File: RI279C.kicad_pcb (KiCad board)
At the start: 2 copper layers, 48.3 x 39.4 mm, 10 parts, among them J1 Ribbon Cable, J2 Multiway, J3 Meter

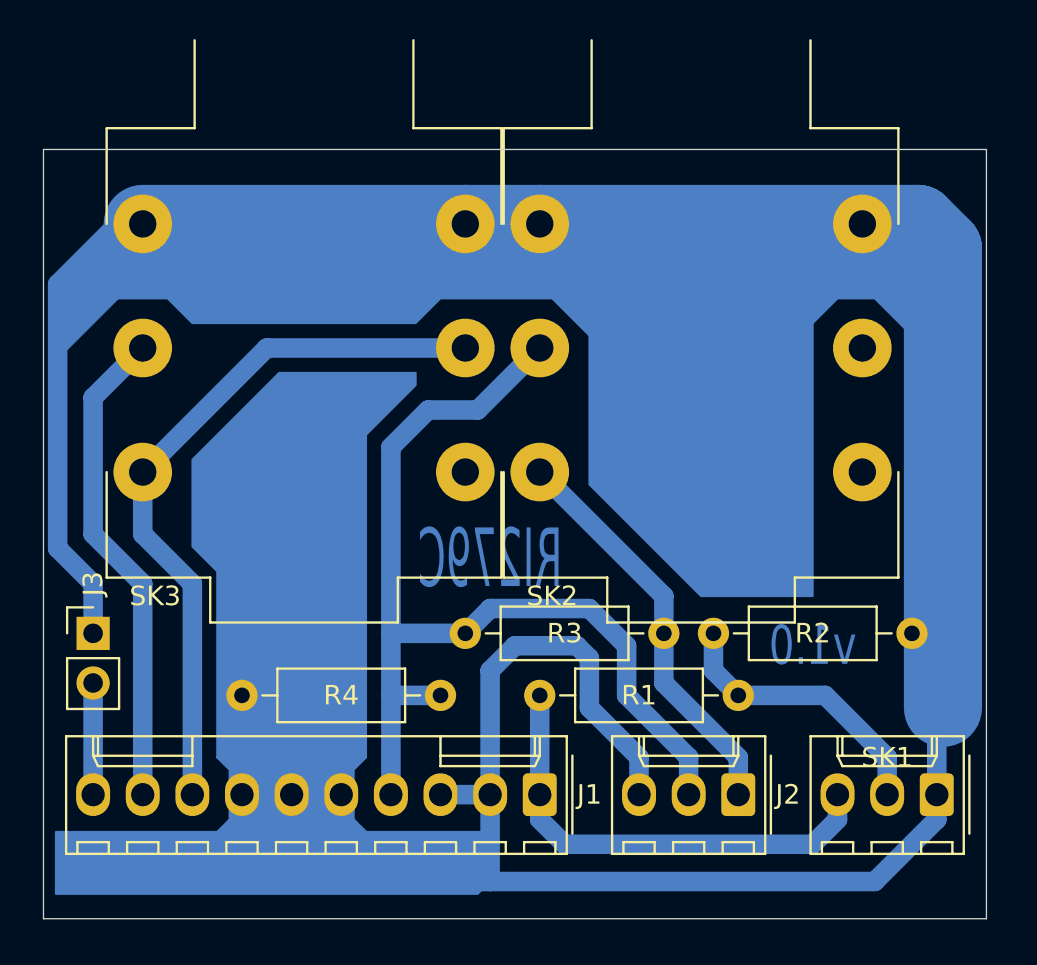
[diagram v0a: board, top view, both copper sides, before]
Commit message: aligned edge cuts to mm grid, 39 mm x 49 mm
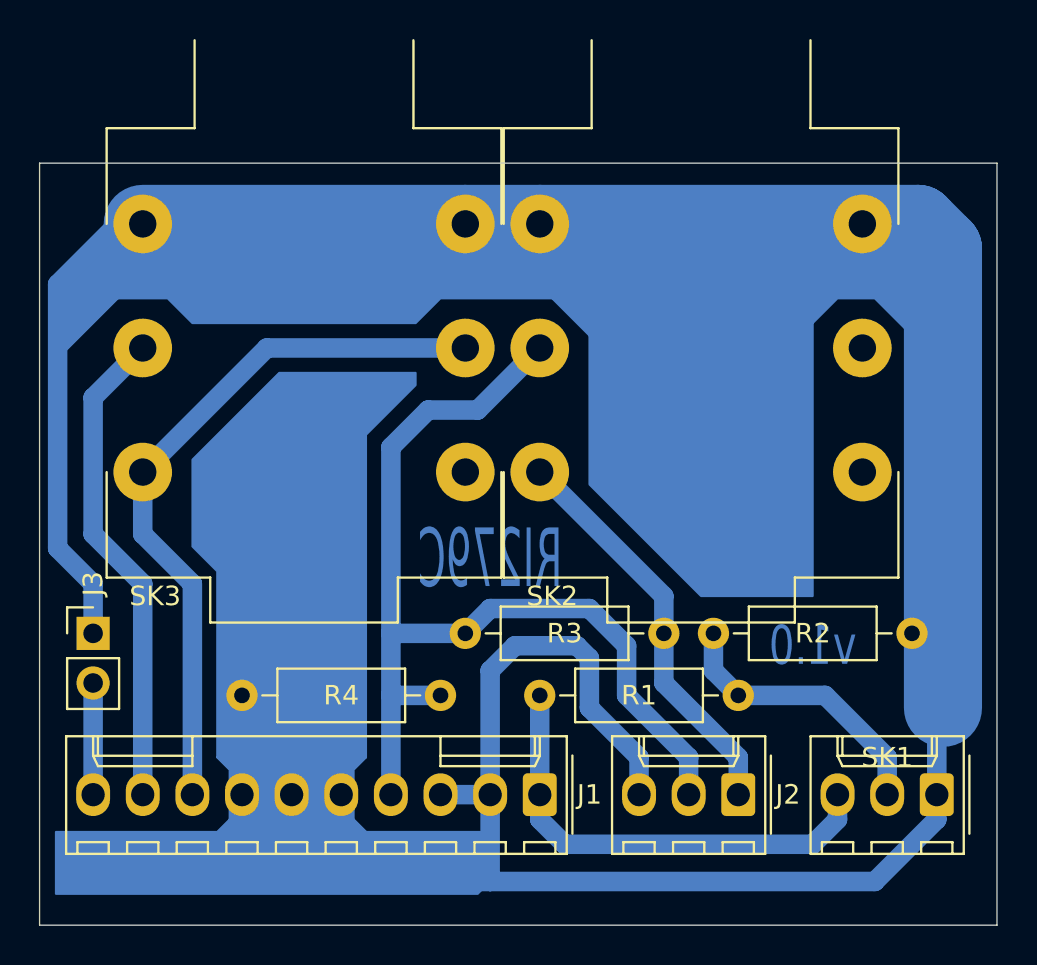
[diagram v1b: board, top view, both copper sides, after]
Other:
- board size 48.3 x 39.4 mm -> 49 x 39 mm
